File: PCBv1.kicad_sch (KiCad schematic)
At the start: 20 parts, among them J1 AVR-ISP-6, SW2 SW_Push_Reset, U1 ATmega32U4-A, Y1 16MHz

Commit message: locked in
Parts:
- removed D1: PRTR5V0U2X, Package_TO_SOT_SMD:SOT-143, symbol Power_Protection:PRTR5V0U2X
- removed F1: 500m, Fuse:Fuse_1206_3216Metric_Pad1.42x1.75mm_HandSolder, symbol Device:Polyfuse_Small
- removed R6, R7: 22, Resistor_SMD:R_0805_2012Metric_Pad1.20x1.40mm_HandSolder, symbol Device:R_Small
- removed R8, R9: 5.1k, Resistor_SMD:R_0805_2012Metric_Pad1.20x1.40mm_HandSolder, symbol Device:R_Small
- removed USB1: HRO-TYPE-C-31-M-12, Type-C:HRO-TYPE-C-31-M-12-HandSoldering, symbol Type-C:HRO-TYPE-C-31-M-12
- added J2: Conn_01x04_MountingPin, Connector_JST:JST_SH_SM04B-SRSS-TB_1x04-1MP_P1.00mm_Horizontal, symbol Connector_Generic_MountingPin:Conn_01x04_MountingPin
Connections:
- net +5V: now also J2.1 (Pin_1)
- net D+: now also J2.3 (Pin_3)
- net D-: now also J2.2 (Pin_2)
- net GND: now also J2.4 (Pin_4), J2.MP (MountPin)
- net MISO: now also U1.10 (PB2); no longer U1.11 (PB3)
- net MOSI: now also U1.8 (PB0); no longer U1.10 (PB2)
- net col7: now also U1.11 (PB3); no longer U1.8 (PB0)
- net row3: now also U1.42 (AREF); no longer U1.1 (PE6)
- net XTAL2: now reaches C7.2, U1.16 (XTAL2), Y1.3
- net XTAL1: now reaches C6.2, U1.17 (XTAL1), Y1.1
- no-connect marks 7 -> 5
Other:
- moved on the sheet: C1, C2, C3, C4, C5, C6, C7, J1, R1, R5, SW2, U1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

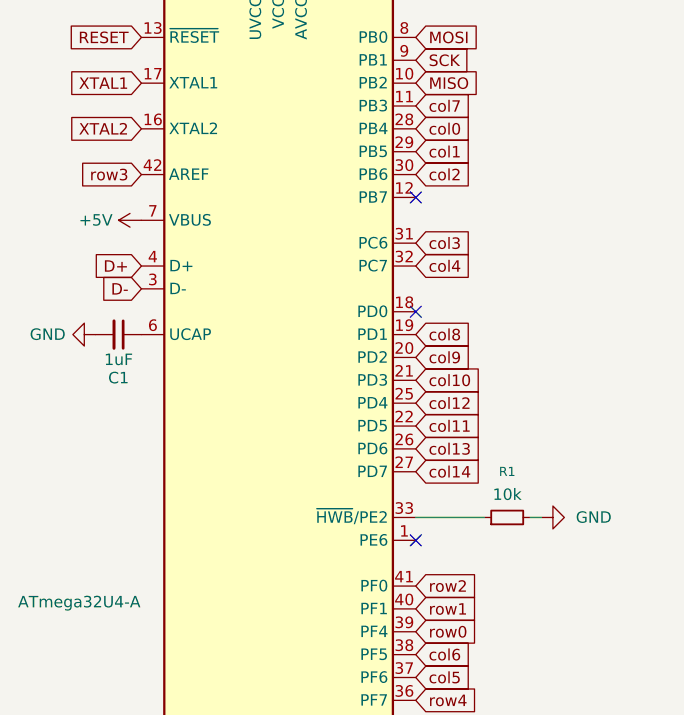
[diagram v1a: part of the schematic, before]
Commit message: fix row3 pin
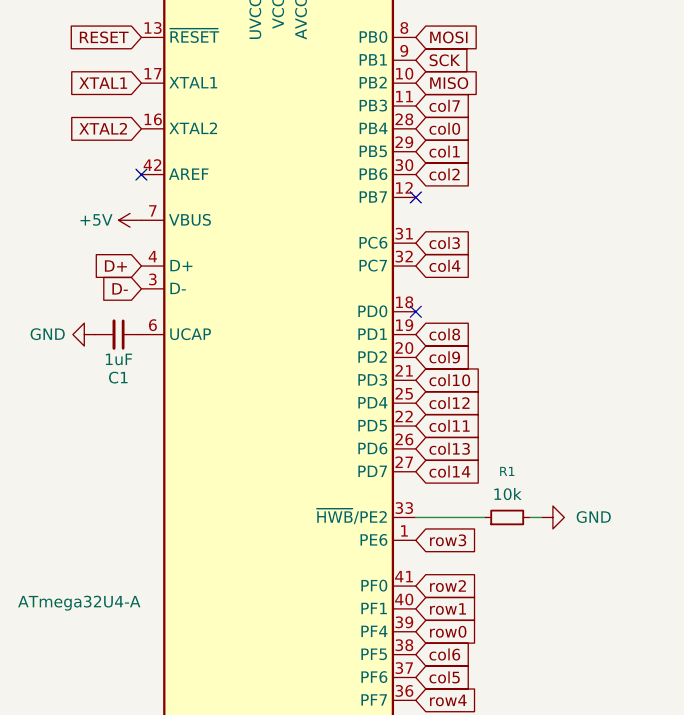
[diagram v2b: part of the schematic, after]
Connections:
- net row3: now also U1.1 (PE6); no longer U1.42 (AREF)
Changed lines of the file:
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@@
 	)
 	(no_connect
-		(at 59.69 87.63)
+		(at 59.69 49.53)
 	)
 	(no_connect
@@
 	)
 	(no_connect
-		(at 59.69 49.53)
+		(at 29.21 46.99)
 	)
 	(no_connect
@@
 	(global_label "row3"
 		(shape input)
-		(at 29.21 46.99 180)
-		(fields_autoplaced yes)
-		(effects
-			(font
-				(size 1.27 1.27)
-			)
-			(justify right)
-		)
-		(property "Intersheetrefs" "${INTERSHEET_REFS}"
-			(at 21.7496 46.99 0)
-			(effects
-				(font
-					(size 1.27 1.27)
-				)
-				(justify right)
-				(hide yes)
-			)
+		(at 59.69 87.63 0)
+		(fields_autoplaced yes)
+		(effects
+			(font
+				(size 1.27 1.27)
+			)
+			(justify left)
+		)
+		(property "Intersheetrefs" "${INTERSHEET_REFS}"
+			(at 67.1504 87.63 0)
+			(effects
+				(font
+					(size 1.27 1.27)
+				)
+				(justify left)
+				(hide yes)
+			)
